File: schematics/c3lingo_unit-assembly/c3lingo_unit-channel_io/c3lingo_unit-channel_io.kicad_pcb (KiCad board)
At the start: 2 copper layers, 75 x 60 mm, 38 parts, among them J601 Mic X In, J602 Headphone X, J603 Interconnect, J604 PowerSupply, U601 NE5534, U602 LM386N-4

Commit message: Update to KiCad 7
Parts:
- removed the H601 at (68.8, 220.4)

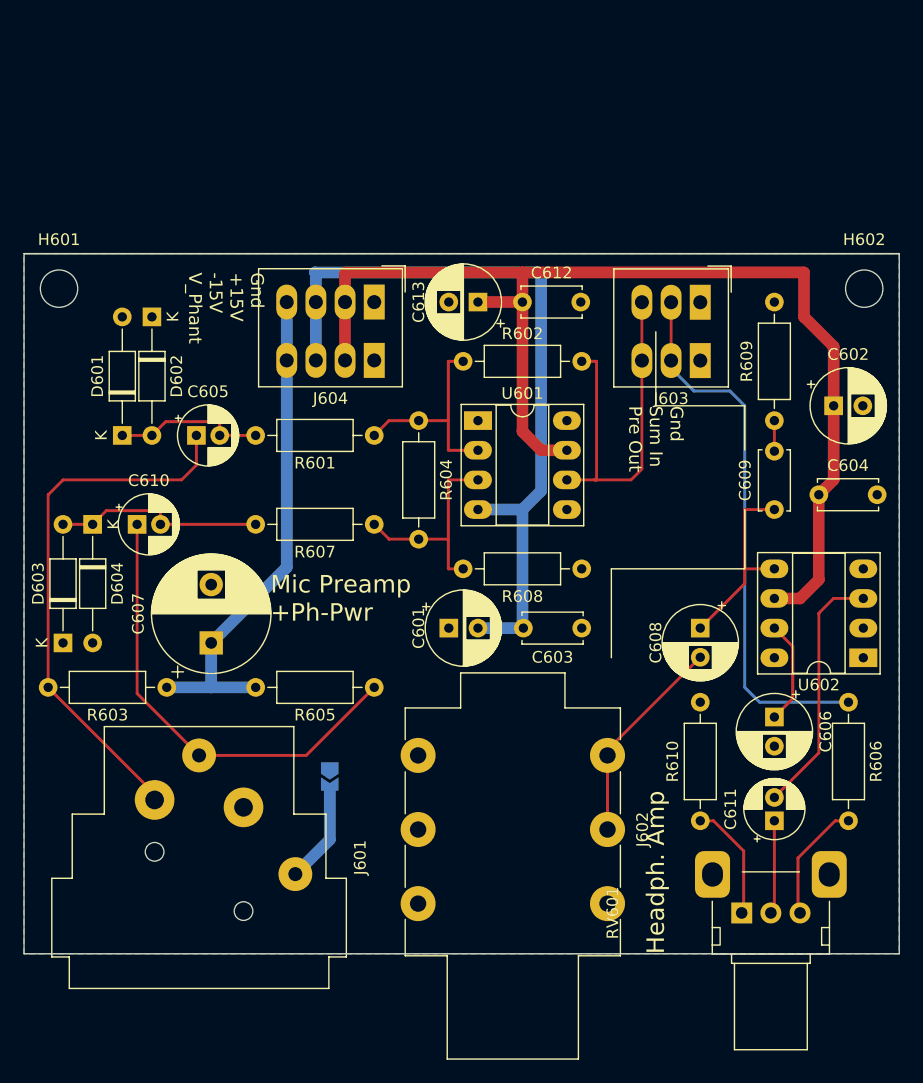
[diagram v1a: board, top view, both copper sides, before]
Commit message: Re-layout boards with SMD components
* Channel Mix: Removed vu meter potentiometer as good setting was found (10 dB
  more headroom)
* Channel Mix: Add vu meter alternate power
* Channel I/O: Added jumper for phantom power enable/disable
* Add GND test points
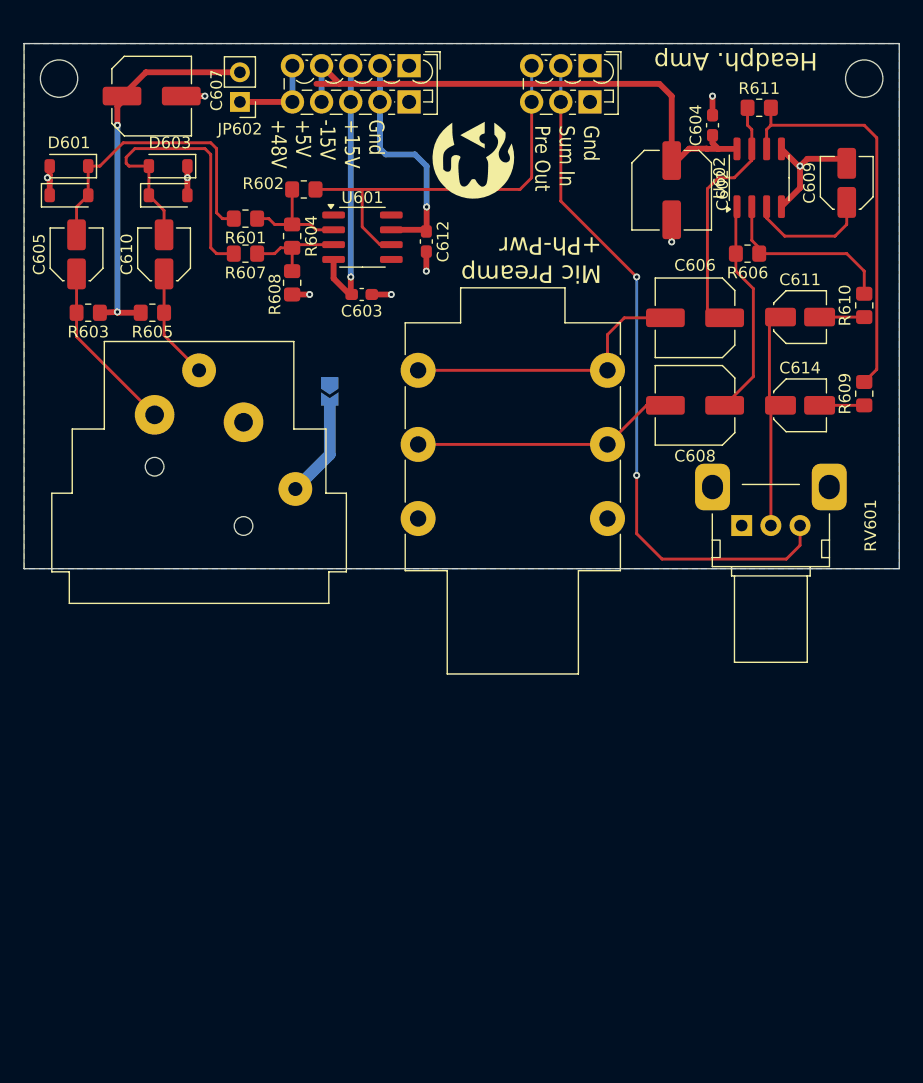
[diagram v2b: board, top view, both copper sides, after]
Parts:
- removed C601, C613: 100uF, Capacitor_THT:CP_Radial_D6.3mm_P2.50mm
- added C614: 1uF, Capacitor_SMD:C_Elec_4x5.8, F.Cu at (116.5, 186.0)
- added G***: LOGO, c3lingo_unit-footprints:voctocat-07mm, F.Cu at (88.5, 165.0)
- added G***: LOGO, c3lingo_unit-footprints:voctocat-25mm, B.Cu at (87.5, 186.0)
- added JP602: Phant. Pwr, Connector_PinHeader_2.54mm:PinHeader_1x02_P2.54mm_Vertical, F.Cu at (68.5, 160.0)
- added R611: 39K, Resistor_SMD:R_0805_2012Metric_Pad1.20x1.40mm_HandSolder, F.Cu at (113.0, 160.5)
- C602: footprint Capacitor_THT:CP_Radial_D6.3mm_P2.50mm -> Capacitor_SMD:C_Elec_6.3x7.7
- C603, C604, C612: value 100nF -> 100nF, lowESR; footprint Capacitor_THT:C_Disc_D5.0mm_W2.5mm_P5.00mm -> Capacitor_SMD:C_0603_1608Metric_Pad1.08x0.95mm_HandSolder
- C605, C610, C611: footprint Capacitor_THT:CP_Radial_D5.0mm_P2.00mm -> Capacitor_SMD:C_Elec_4x5.8
- C606: value 100uF -> 68uF lowESR; footprint Capacitor_THT:CP_Radial_D6.3mm_P2.50mm -> Capacitor_SMD:C_Elec_6.3x5.8
- C607: footprint Capacitor_THT:CP_Radial_D10.0mm_P5.00mm -> Capacitor_SMD:C_Elec_6.3x7.7
- C608: value 220uF lowESR -> 68uF lowESR; footprint Capacitor_THT:CP_Radial_D6.3mm_P2.50mm -> Capacitor_SMD:C_Elec_6.3x5.8
- C609: value 47nF -> 1uF lowESR; footprint Capacitor_THT:C_Disc_D5.0mm_W2.5mm_P5.00mm -> Capacitor_SMD:C_Elec_4x5.8
- D601, D602, D603, D604: footprint Diode_THT:D_DO-35_SOD27_P10.16mm_Horizontal -> Diode_SMD:D_SOD-123
- J603: footprint TerminalBlock_Phoenix:TerminalBlock_Phoenix_PTSM-0,5-3-2.5-H-THR_1x03_P2.50mm_Horizontal -> TerminalBlock_Phoenix:TerminalBlock_Phoenix_PTSM-0,5-3-2.5-V-THR_1x03_P2.50mm_Vertical
- J604: footprint TerminalBlock_Phoenix:TerminalBlock_Phoenix_PTSM-0,5-4-2.5-H-THR_1x04_P2.50mm_Horizontal -> TerminalBlock_Phoenix:TerminalBlock_Phoenix_PTSM-0,5-5-2.5-V-THR_1x05_P2.50mm_Vertical
- R601, R602, R603, R604, R605, R607, R608: footprint Resistor_THT:R_Axial_DIN0207_L6.3mm_D2.5mm_P10.16mm_Horizontal -> Resistor_SMD:R_0805_2012Metric_Pad1.20x1.40mm_HandSolder
- R606: value 330K -> 39K; footprint Resistor_THT:R_Axial_DIN0207_L6.3mm_D2.5mm_P10.16mm_Horizontal -> Resistor_SMD:R_0805_2012Metric_Pad1.20x1.40mm_HandSolder
- R609: value 12R -> 10K; footprint Resistor_THT:R_Axial_DIN0207_L6.3mm_D2.5mm_P10.16mm_Horizontal -> Resistor_SMD:R_0805_2012Metric_Pad1.20x1.40mm_HandSolder
- R610: value 2.2K -> 10K; footprint Resistor_THT:R_Axial_DIN0207_L6.3mm_D2.5mm_P10.16mm_Horizontal -> Resistor_SMD:R_0805_2012Metric_Pad1.20x1.40mm_HandSolder
- U601: footprint Package_DIP:DIP-8_W7.62mm_Socket_LongPads -> Package_SO:SOIC-8_3.9x4.9mm_P1.27mm
- U602: value LM386N-4 -> TPA6111A2; footprint Package_DIP:DIP-8_W7.62mm_Socket_LongPads -> Package_SO:SOIC-8_3.9x4.9mm_P1.27mm
- moved C607 47.1 mm to (60.9, 159.5), turned to 0 degrees
- moved R610 46.3 mm to (122.0, 177.4)
- moved C611 43.2 mm to (116.5, 178.4), turned to 0 degrees
- moved U602 42.1 mm to (113.0, 166.5), turned to 90 degrees
- moved D603 41.8 mm to (62.4, 165.5), turned to 180 degrees
- moved R606 39.4 mm to (112.0, 173.0), turned to 180 degrees
- moved R605 37.3 mm to (61.0, 178.1)
- moved C606 34.9 mm to (107.5, 178.5), turned to 180 degrees
- moved R608 34.9 mm to (73.0, 175.5), turned to 90 degrees
- moved C603 34.2 mm to (78.9, 176.5)
- moved RV601 33.2 mm to (111.5, 196.3)
- moved J601 33.0 mm to (68.8, 187.4)
- moved J602 33.0 mm to (100.0, 183.0)
- moved JP601 33.0 mm to (76.2, 184.8)
- moved C604 32.9 mm to (109.0, 162.0), turned to 90 degrees
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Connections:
- C602 pad 1: +15V -> +5V
- C604 pad 1: +15V -> +5V
- C606 pad 2: GND -> Net-(C606-Pad2)
- C608 pad 1: Net-(C608-Pad1) -> Net-(U602-VO1)
- C609 pad 1: Net-(C608-Pad1) -> Net-(U602-BYPASS)
- C609 pad 2: Net-(C609-Pad2) -> GND
- C611 pad 2: Net-(U602-+) -> Net-(C611-Pad2)
- J602 pad RN: (no net) -> Net-(C608-Pad2)
- J602 pad SN: (no net) -> GND
- J602 pad T: Net-(C608-Pad2) -> Net-(C606-Pad2)
- J602 pad TN: (no net) -> Net-(C606-Pad2)
- J604 pad 4: V_Phant -> +5V
- R606 pad 1: /HeadphoneAmpIn -> Net-(U602-IN1-)
- R606 pad 2: Net-(R606-Pad2) -> Net-(U602-VO1)
- R609 pad 1: Net-(C609-Pad2) -> Net-(C614-Pad2)
- R609 pad 2: GND -> Net-(U602-IN2-)
- R610 pad 1: Net-(R610-Pad1) -> Net-(C611-Pad2)
- R610 pad 2: GND -> Net-(U602-IN1-)
- RV601 pad 1: Net-(R610-Pad1) -> GND
- RV601 pad 3: Net-(R606-Pad2) -> /HeadphoneAmpIn
- U602 pad 1: unconnected-(U602-GAIN-Pad1) -> Net-(U602-VO1)
- U602 pad 2: GND -> Net-(U602-IN1-)
- U602 pad 3: Net-(U602-+) -> Net-(U602-BYPASS)
- U602 pad 5: Net-(C608-Pad1) -> GND
- U602 pad 6: +15V -> Net-(U602-IN2-)
- U602 pad 8: unconnected-(U602-GAIN-Pad8) -> +5V
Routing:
- net +15V: track 101.1 -> 20.2 mm, vias 0 -> 1
- net +5V: track 0.00 -> 49.8 mm
- net -15V: track 65.6 -> 23.2 mm, vias 0 -> 1
- net Net-(U602-IN2-): track 0.00 -> 34.6 mm
- net Net-(C605-Pad1): track 46.2 -> 14.5 mm
- net Net-(C610-Pad1): track 39.4 -> 9.12 mm
- net GND: track 0.00 -> 26.8 mm, vias 0 -> 9
- net Net-(C606-Pad2): track 0.00 -> 24.3 mm
- net Net-(U602-+): track 21.7 -> 0.00 mm
- net Net-(U602-VO1): track 0.00 -> 18.7 mm
- net Net-(C608-Pad1): track 16.8 -> 0.00 mm
- net Net-(U602-IN1-): track 0.00 -> 15.8 mm
- net /HeadphoneAmpIn: track 46.9 -> 59.9 mm, vias 0 -> 2
- net Net-(D601-K): track 13.1 -> 25.1 mm
- net Net-(U602-VO2): track 8.92 -> 20.5 mm
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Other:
- board size 75 x 60 mm -> 75 x 45 mm
- board text added: "Gnd +15V -15V +5V +48V"
- board text added: "c3lingo Interpreter Unit Channel I/O v0.3 2024-07-06"
- board text removed: "Gnd +15V -15V V_Phant"
- board text removed: "c3lingo Interpreter Unit v0.3 2023-12-30 Jannik Beyerstedt (jtbx)"

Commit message: Channel-Mix: Rework LED supply voltage
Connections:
- J602 pad R: Net-(C608-Pad2) -> Net-(C606-Pad2)
- J602 pad RN: Net-(C608-Pad2) -> Net-(C606-Pad2)
- J602 pad T: Net-(C606-Pad2) -> Net-(C608-Pad2)
- J602 pad TN: Net-(C606-Pad2) -> Net-(C608-Pad2)
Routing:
- net Net-(C606-Pad2): track 24.3 -> 41.9 mm
- net Net-(C608-Pad2): track 22.1 -> 23.5 mm
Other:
- board text added: "c3lingo Interpreter Unit Channel I/O v0.3 2024-07-07"
- board text removed: "c3lingo Interpreter Unit Channel I/O v0.3 2024-07-06"
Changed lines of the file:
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@@
 	(title_block
 		(title "c3lingo interpeter unit -- channel strip")
-		(date "2022-12-31")
+		(date "2024-07-07")
 		(rev "v0.3")
 		(company "Jannik Beyerstedt (jtbx)")
@@
 			(layers "*.Cu" "*.Mask")
 			(remove_unused_layers no)
-			(net 8 "Net-(C608-Pad2)")
+			(net 14 "Net-(C606-Pad2)")
 			(pintype "passive")
 		)
@@
 			(layers "*.Cu" "*.Mask")
 			(remove_unused_layers no)
-			(net 8 "Net-(C608-Pad2)")
+			(net 14 "Net-(C606-Pad2)")
+			(pintype "passive")
 		)
 		(pad "S" thru_hole circle
@@
 			(remove_unused_layers no)
 			(net 3 "GND")
+			(pintype "passive")
 		)
 		(pad "T" thru_hole circle
@@
 			(layers "*.Cu" "*.Mask")
 			(remove_unused_layers no)
-			(net 14 "Net-(C606-Pad2)")
+			(net 8 "Net-(C608-Pad2)")
 			(pintype "passive")
 		)
@@
 			(layers "*.Cu" "*.Mask")
 			(remove_unused_layers no)
-			(net 14 "Net-(C606-Pad2)")
+			(net 8 "Net-(C608-Pad2)")
+			(pintype "passive")
 		)
 		(model "${KICAD8_3DMODEL_DIR}/Connector_Audio.3dshapes/Jack_6.35mm_Neutrik_NMJ6HFD2_Horizontal.wrl"
@@
 		(layer "Edge.Cuts")
 	)
-	(gr_text "c3lingo Interpreter Unit\nChannel I/O\nv0.3 2024-07-06"
+	(gr_text "c3lingo Interpreter Unit\nChannel I/O\nv0.3 2024-07-07"
 		(at 88.5 170 180)
 		(layer "B.SilkS")
@@
 	)
 	(gr_text "Gnd\n+15V\n-15V\n+5V\n+48V"
-		(at 76 161.5 270)
+		(at 78 161.5 270)
 		(layer "F.SilkS")
 		(effects
@@
 	)
 	(segment
-		(start 100 189.35)
-		(end 103.35 186)
+		(start 103 186)
+		(end 100 183)
 		(width 0.25)
 		(layer "F.Cu")
@@
 	)
 	(segment
-		(start 100 189.35)
-		(end 83.77 189.35)
+		(start 104.9625 186)
+		(end 103 186)
 		(width 0.25)
 		(layer "F.Cu")
@@
 	)
 	(segment
+		(start 83.77 183)
+		(end 100 183)
+		(width 0.25)
+		(layer "B.Cu")
+		(net 8)
+	)
+	(segment
 		(start 58 162)
 		(end 58 160.375)
@@
 	)
 	(segment
-		(start 101.4375 178.5)
-		(end 104.4375 178.5)
-		(width 0.25)
-		(layer "F.Cu")
-		(net 14)
-	)
-	(segment
-		(start 100 179.9375)
-		(end 101.4375 178.5)
+		(start 104.9625 178.5)
+		(end 94.62 178.5)
 		(width 0.25)
 		(layer "F.Cu")
@@
 	)
 	(segment
-		(start 100 183)
-		(end 83.77 183)
+		(start 94.62 178.5)
+		(end 83.77 189.35)
 		(width 0.25)
 		(layer "F.Cu")
@@
 	)
 	(segment
-		(start 100 179.9375)
-		(end 100 183)
+		(start 83.77 189.35)
+		(end 100 189.35)
 		(width 0.25)
-		(layer "F.Cu")
+		(layer "B.Cu")
 		(net 14)
 	)

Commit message: Channel I/O: Fix headphone amp caps, re-phrase readme section
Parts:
- G***: footprint c3lingo_unit-footprints:voctocat-25mm -> c3lingo_unit-footprints:voctocat-15mm
- moved G*** 11.0 mm to (87.5, 175.0)
- moved G*** 0.50 mm to (89.0, 165.0)
- turned C611 to 180 degrees
- turned C614 to 180 degrees
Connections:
- C614 pad 1: Net-(C611-Pad1) -> Net-(C614-Pad1)
- C614 pad 2: Net-(C614-Pad2) -> Net-(C611-Pad2)
- R609 pad 1: Net-(C614-Pad2) -> Net-(C614-Pad1)
- R610 pad 1: Net-(C611-Pad2) -> Net-(C611-Pad1)
- RV601 pad 2: Net-(C611-Pad1) -> Net-(C611-Pad2)
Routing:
- net Net-(C611-Pad2): track 4.00 -> 17.9 mm
- net Net-(C611-Pad1): track 17.9 -> 4.00 mm
- net Net-(C614-Pad2): track 4.00 -> 0.00 mm
- net Net-(C614-Pad1): track 0.00 -> 4.00 mm
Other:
- board text added: "c3lingo Interpreter Unit Channel I/O v0.3.1 2024-07-08"
- board text removed: "c3lingo Interpreter Unit Channel I/O v0.3 2024-07-07"

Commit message: Tidy: Rename hierarchical labels
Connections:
- net /HeadphoneAmpIn renamed /Headphone
- net /MicPreOut renamed /MicPre
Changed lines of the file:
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@@
 	(net 18 "Net-(U602-VO1)")
 	(net 19 "Net-(C611-Pad2)")
-	(net 20 "/HeadphoneAmpIn")
-	(net 21 "/MicPreOut")
+	(net 20 "/Headphone")
+	(net 21 "/MicPre")
 	(net 22 "unconnected-(U601-BAL-Pad1)")
 	(net 23 "unconnected-(U601-COMP-Pad5)")
@@
 			(layers "F.Cu" "F.Paste" "F.Mask")
 			(roundrect_rratio 0.25)
-			(net 21 "/MicPreOut")
+			(net 21 "/MicPre")
 			(pintype "output")
 		)
@@
 			(layers "*.Cu" "*.Mask")
 			(remove_unused_layers no)
-			(net 20 "/HeadphoneAmpIn")
+			(net 20 "/Headphone")
 			(pinfunction "Pin_2")
 			(pintype "passive")
@@
 			(layers "*.Cu" "*.Mask")
 			(remove_unused_layers no)
-			(net 20 "/HeadphoneAmpIn")
+			(net 20 "/Headphone")
 			(pinfunction "Pin_2")
 			(pintype "passive")
@@
 			(layers "*.Cu" "*.Mask")
 			(remove_unused_layers no)
-			(net 21 "/MicPreOut")
+			(net 21 "/MicPre")
 			(pinfunction "Pin_3")
 			(pintype "passive")
@@
 			(layers "*.Cu" "*.Mask")
 			(remove_unused_layers no)
-			(net 21 "/MicPreOut")
+			(net 21 "/MicPre")
 			(pinfunction "Pin_3")
 			(pintype "passive")
@@
 			(layers "*.Cu" "*.Mask")
 			(remove_unused_layers no)
-			(net 20 "/HeadphoneAmpIn")
+			(net 20 "/Headphone")
 			(pinfunction "3")
 			(pintype "passive")
@@
 			(layers "F.Cu" "F.Paste" "F.Mask")
 			(roundrect_rratio 0.208333)
-			(net 21 "/MicPreOut")
+			(net 21 "/MicPre")
 			(pintype "passive")
 		)

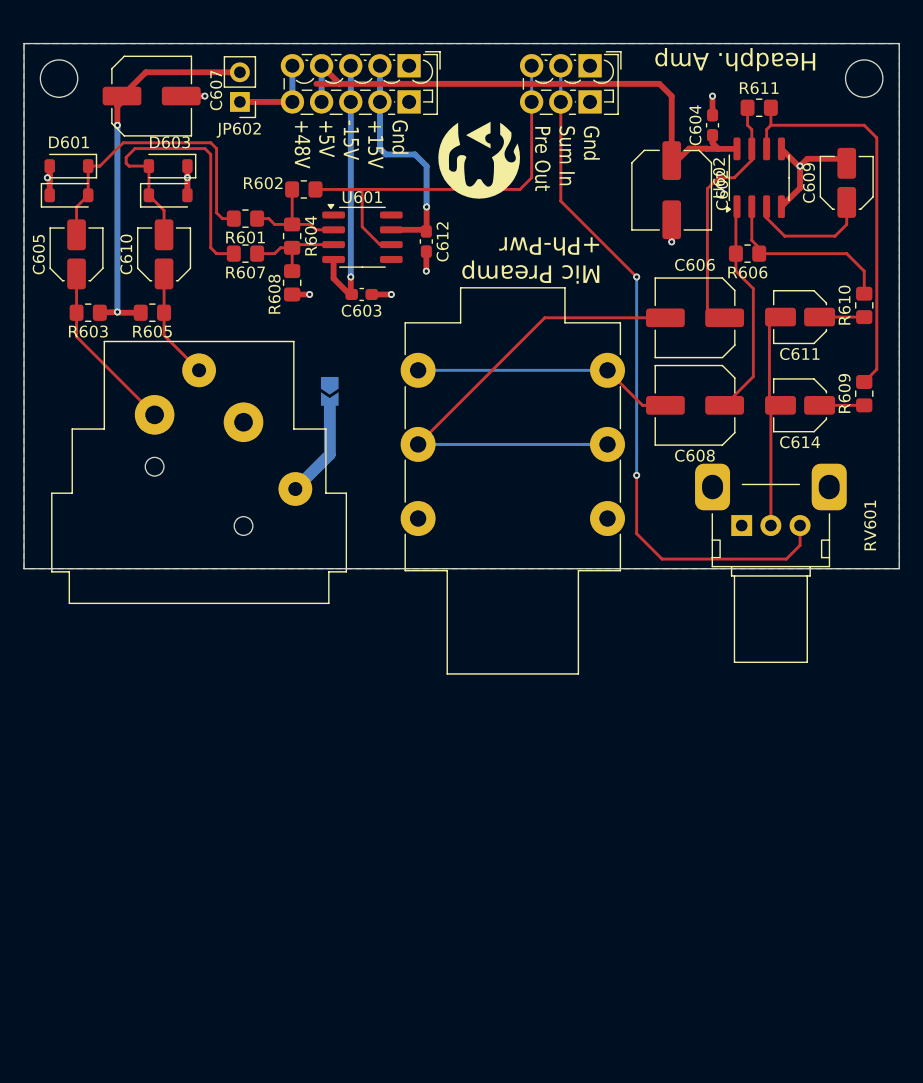
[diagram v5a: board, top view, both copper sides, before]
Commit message: Channel Mixer: Rework muting mechanism
Note: Schematic PDF not updated yet
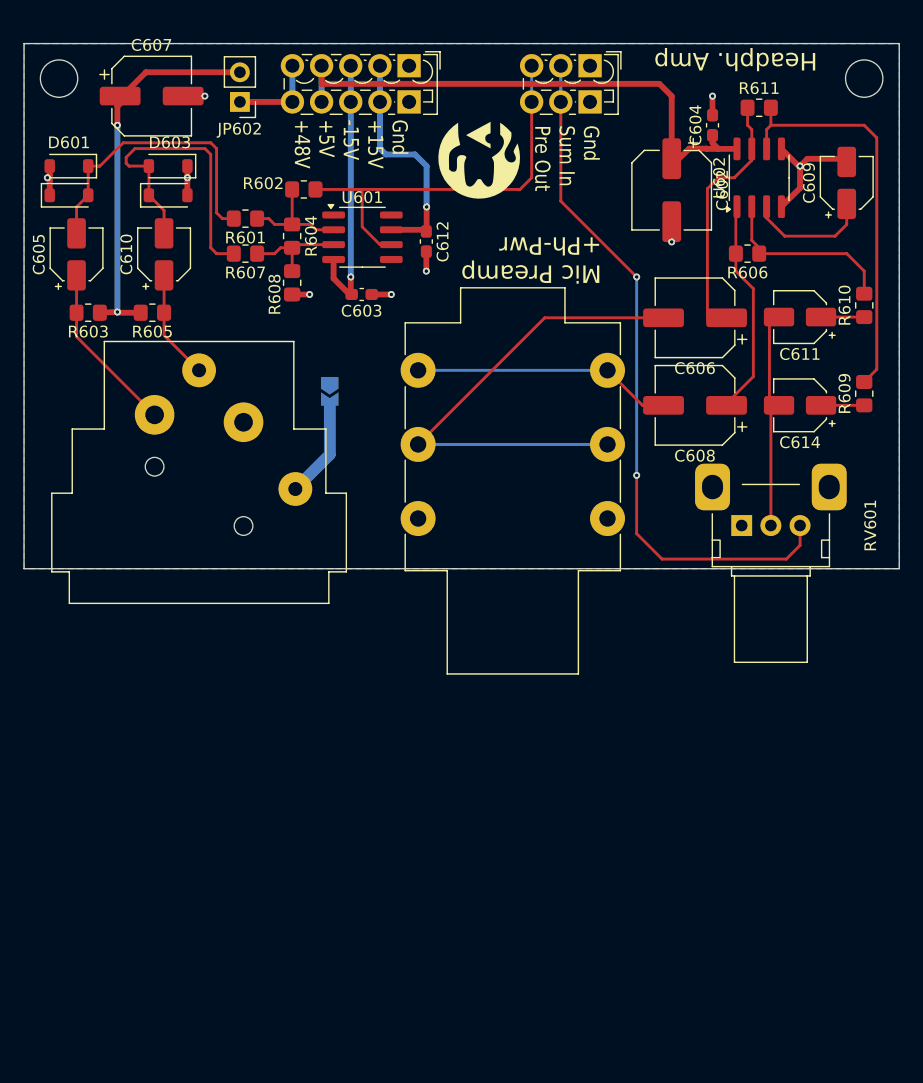
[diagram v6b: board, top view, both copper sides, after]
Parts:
- C602, C607: footprint Capacitor_SMD:C_Elec_6.3x7.7 -> Capacitor_SMD:CP_Elec_6.3x7.7
- C605, C609, C610, C611, C614: footprint Capacitor_SMD:C_Elec_4x5.8 -> Capacitor_SMD:CP_Elec_4x5.8
- C606, C608: footprint Capacitor_SMD:C_Elec_6.3x5.8 -> Capacitor_SMD:CP_Elec_6.3x5.8
- R602, R608: value 330K 1% -> 68K 1%
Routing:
- net +5V: track 49.8 -> 48.7 mm
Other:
- board text added: "c3lingo Interpreter Unit Channel I/O v0.3.1 2024-08-30"
- board text removed: "c3lingo Interpreter Unit Channel I/O v0.3.1 2024-07-08"
